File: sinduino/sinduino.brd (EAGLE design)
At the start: 100 x 80 mm, 34 parts, among them IC1 IC_UC_ATMEGA32U4-TQFP44, IC2 TS2940CT5TV, Q1 16000, X1 MINI-USB-32005-301

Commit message: move some things around in the upper right
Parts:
- moved LED4 9.85 mm to (51.8, 18.1)
- moved R3 4.26 mm to (32.4, 27.3), turned to 180 degrees
- moved C4 2.56 mm to (54.0, 21.3)
- moved R6 2.42 mm to (47.9, 21.3), turned to 180 degrees
- moved C3 1.93 mm to (34.3, 25.1)
- moved C9 1.62 mm to (42.2, 25.1)
- moved C8 1.27 mm to (48.3, 24.8)
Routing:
- net VCC: track 109.5 -> 115.7 mm
- net N$18: track 0.00 -> 2.92 mm
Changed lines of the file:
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@@
 <setting verticaltext="up"/>
 </settings>
-<grid distance="12.5" unitdist="mil" unit="mil" style="dots" multiple="1" display="no" altdistance="25" altunitdist="mil" altunit="mil"/>
+<grid distance="12.5" unitdist="mil" unit="mil" style="dots" multiple="1" display="yes" altdistance="25" altunitdist="mil" altunit="mil"/>
 <layers>
 <layer number="1" name="Top" color="4" fill="1" visible="yes" active="yes"/>
@@
 <element name="C1" library="rcl" package="C025-025X050" value="470n" x="12.7" y="27.94" rot="R270"/>
 <element name="C2" library="rcl" package="E2,5-6" value="33u" x="12.7" y="22.225" rot="R90"/>
-<element name="C3" library="rcl" package="C1206" value="100n" x="36.195" y="24.765" rot="MR180"/>
-<element name="C4" library="rcl" package="C1206" value="100n" x="55.245" y="23.495" rot="MR0"/>
+<element name="C3" library="rcl" package="C1206" value="100n" x="34.29" y="25.0825" rot="MR180"/>
+<element name="C4" library="rcl" package="C1206" value="100n" x="53.975" y="21.2725" rot="MR0"/>
 <element name="C5" library="rcl" package="C1206" value="100n" x="42.8625" y="8.89" rot="MR180"/>
 <element name="C6" library="rcl" package="C1206" value="100n" x="24.13" y="10.4775" rot="MR0"/>
 <element name="C7" library="rcl" package="C1206" value="100n" x="23.1775" y="7.62" rot="MR0"/>
-<element name="C8" library="rcl" package="C1206" value="18p" x="48.26" y="23.495" rot="MR0"/>
-<element name="C9" library="rcl" package="C1206" value="18p" x="42.545" y="23.495" rot="MR0"/>
+<element name="C8" library="rcl" package="C1206" value="18p" x="48.26" y="24.765" rot="MR0"/>
+<element name="C9" library="rcl" package="C1206" value="18p" x="42.2275" y="25.0825" rot="MR0"/>
 <element name="C10" library="rcl" package="C1206" value="1u" x="22.86" y="19.05" rot="MR0"/>
 <element name="C11" library="rcl" package="C1206" value="1u" x="15.875" y="6.985" rot="MR180"/>
@@
 <attribute name="REICHELT" value="TASTER 9305" x="28.8925" y="26.035" size="1.778" layer="27" rot="R270" display="off"/>
 </element>
-<element name="R3" library="rcl" package="R1206" value="10k" x="36.195" y="29.21" rot="MR270"/>
+<element name="R3" library="rcl" package="R1206" value="10k" x="32.385" y="27.305" rot="MR180"/>
 <element name="X1" library="con-cypressindustries" package="32005-301" value="MINI-USB-32005-301" x="6" y="18.5" rot="MR180">
 <attribute name="OC_NEWARK" value="unknown" x="6" y="18.5" size="1.778" layer="28" rot="MR180" display="off"/>
@@
 <element name="JP2" library="pinhead" package="1X17" value="" x="30" y="33"/>
 <element name="JP3" library="pinhead" package="1X17" value="" x="30" y="4" rot="R180"/>
-<element name="R6" library="rcl" package="R1206" value="680" x="50.165" y="20.32" rot="MR0"/>
-<element name="LED4" library="led" package="LED3MM" value="yellow" x="55.245" y="27.305" rot="R180"/>
+<element name="R6" library="rcl" package="R1206" value="680" x="47.9425" y="21.2725" rot="MR180"/>
+<element name="LED4" library="led" package="LED3MM" value="yellow" x="51.7525" y="18.0975" rot="R180"/>
 <element name="R5" library="rcl" package="R1206" value="3k9" x="46.6725" y="10.4775" rot="MR90"/>
 <element name="IC2" library="n39" package="TO220V" value="TS2940CT5TV" x="20.32" y="25.0825" rot="R270">
@@
 <wire x1="9.68" y1="33" x2="9.68" y2="31.5875" width="0.4064" layer="16"/>
 <wire x1="9.68" y1="31.5875" x2="8.255" y2="30.1625" width="0.4064" layer="16"/>
-<wire x1="56.645" y1="23.495" x2="56.515" y2="27.305" width="0" layer="19" extent="16-16"/>
-<wire x1="42.53" y1="19.71" x2="56.645" y2="23.495" width="0" layer="19" extent="16-16"/>
+<wire x1="33.807" y1="27.305" x2="33.807" y2="25.9995" width="0.4064" layer="16"/>
+<wire x1="33.807" y1="25.9995" x2="32.89" y2="25.0825" width="0.4064" layer="16"/>
+<wire x1="34.43" y1="22.21" x2="34.43" y2="23.5425" width="0.4064" layer="16"/>
+<wire x1="34.43" y1="23.5425" x2="32.89" y2="25.0825" width="0.4064" layer="16"/>
+<wire x1="53.0225" y1="18.0975" x2="55.375" y2="21.2725" width="0" layer="19" extent="16-16"/>
+<wire x1="42.53" y1="19.71" x2="53.0225" y2="18.0975" width="0" layer="19" extent="16-16"/>
 <wire x1="34.43" y1="19.5075" x2="40.83" y2="19.24" width="0" layer="19" extent="16-16"/>
-<wire x1="34.795" y1="24.765" x2="34.43" y2="22.21" width="0" layer="19" extent="16-16"/>
-<wire x1="36.195" y1="27.788" x2="34.795" y2="24.765" width="0" layer="19" extent="16-16"/>
 <wire x1="32.0925" y1="13.31" x2="32.2325" y2="17.31" width="0" layer="19" extent="16-16"/>
 </signal>
@@
 <contactref element="IC1" pad="P17"/>
 <contactref element="Q1" pad="2"/>
-<wire x1="46.86" y1="23.495" x2="48.768" y2="28.575" width="0" layer="19" extent="16-16"/>
-<wire x1="36.83" y1="22.21" x2="46.86" y2="23.495" width="0" layer="19" extent="16-16"/>
+<wire x1="46.86" y1="24.765" x2="48.768" y2="28.575" width="0" layer="19" extent="16-16"/>
+<wire x1="36.83" y1="22.21" x2="46.86" y2="24.765" width="0" layer="19" extent="16-16"/>
 </signal>
 <signal name="N$4">
@@
 <contactref element="C9" pad="2"/>
 <contactref element="Q1" pad="1"/>
-<wire x1="41.145" y1="23.495" x2="43.942" y2="28.575" width="0" layer="19" extent="16-16"/>
-<wire x1="36.03" y1="22.21" x2="41.145" y2="23.495" width="0" layer="19" extent="16-16"/>
+<wire x1="40.8275" y1="25.0825" x2="43.942" y2="28.575" width="0" layer="19" extent="16-16"/>
+<wire x1="36.03" y1="22.21" x2="40.8275" y2="25.0825" width="0" layer="19" extent="16-16"/>
 </signal>
 <signal name="N$6">
@@
 <wire x1="32.54" y1="31.905" x2="31.1425" y2="30.5075" width="0.4064" layer="16"/>
 <wire x1="31.1425" y1="29.285" x2="31.1425" y2="30.5075" width="0.4064" layer="16"/>
-<wire x1="31.1425" y1="29.285" x2="31.1425" y2="22.785" width="0.4064" layer="16"/>
 <wire x1="33.63" y1="22.21" x2="33.63" y2="23.2025" width="0.4064" layer="16"/>
 <wire x1="33.63" y1="23.2025" x2="33.3375" y2="23.495" width="0.4064" layer="16"/>
 <wire x1="33.3375" y1="23.495" x2="31.8525" y2="23.495" width="0.4064" layer="16"/>
+<wire x1="31.1425" y1="29.285" x2="31.1425" y2="27.4845" width="0.4064" layer="16"/>
+<wire x1="31.1425" y1="27.4845" x2="30.963" y2="27.305" width="0.4064" layer="16"/>
+<wire x1="31.1425" y1="22.785" x2="31.1425" y2="27.1255" width="0.4064" layer="16"/>
+<wire x1="31.1425" y1="27.1255" x2="30.963" y2="27.305" width="0.4064" layer="16"/>
 <wire x1="31.8525" y1="23.495" x2="31.1425" y2="22.785" width="0.4064" layer="16"/>
-<wire x1="32.54" y1="31.905" x2="36.195" y2="30.632" width="0" layer="19" extent="16-16"/>
 </signal>
 <signal name="N$8">
@@
 <contactref element="IC1" pad="P22"/>
 <contactref element="R6" pad="1"/>
-<wire x1="40.83" y1="22.21" x2="51.587" y2="20.32" width="0" layer="19" extent="16-16"/>
+<wire x1="40.83" y1="22.21" x2="46.5205" y2="21.2725" width="0" layer="19" extent="16-16"/>
 </signal>
 <signal name="N$11">
 <contactref element="R6" pad="2"/>
 <contactref element="LED4" pad="K"/>
-<wire x1="48.743" y1="20.32" x2="53.975" y2="27.305" width="0" layer="19" extent="16-16"/>
+<wire x1="50.4825" y1="18.0975" x2="49.3645" y2="21.2725" width="0" layer="19" extent="16-16"/>
 </signal>
 <signal name="D7">
@@
 <contactref element="IC1" pad="P42"/>
 <contactref element="C7" pad="1"/>
-<wire x1="34.43" y1="10.81" x2="34.43" y2="9.3475" width="0.4064" layer="16"/>
-<wire x1="34.43" y1="9.3475" x2="33.9725" y2="8.89" width="0.4064" layer="16"/>
-<wire x1="33.9725" y1="8.89" x2="27.6225" y2="8.89" width="0.4064" layer="16"/>
-<wire x1="27.6225" y1="8.89" x2="26.3525" y2="7.62" width="0.4064" layer="16"/>
-<wire x1="26.3525" y1="7.62" x2="24.5775" y2="7.62" width="0.4064" layer="16"/>
-<wire x1="22.38" y1="4" x2="22.38" y2="5.235" width="0.4064" layer="16"/>
-<wire x1="22.38" y1="5.235" x2="24.5775" y2="7.4325" width="0.4064" layer="16"/>
-<wire x1="24.5775" y1="7.4325" x2="24.5775" y2="7.62" width="0.4064" layer="16"/>
+<wire x1="34.43" y1="10.81" x2="34.43" y2="9.3475" width="0.3048" layer="16"/>
+<wire x1="34.43" y1="9.3475" x2="33.9725" y2="8.89" width="0.3048" layer="16"/>
+<wire x1="33.9725" y1="8.89" x2="27.6225" y2="8.89" width="0.3048" layer="16"/>
+<wire x1="27.6225" y1="8.89" x2="26.3525" y2="7.62" width="0.3048" layer="16"/>
+<wire x1="26.3525" y1="7.62" x2="24.5775" y2="7.62" width="0.3048" layer="16"/>
+<wire x1="22.38" y1="4" x2="22.38" y2="5.235" width="0.3048" layer="16"/>
+<wire x1="22.38" y1="5.235" x2="24.5775" y2="7.4325" width="0.3048" layer="16"/>
+<wire x1="24.5775" y1="7.4325" x2="24.5775" y2="7.62" width="0.3048" layer="16"/>
 </signal>
 <signal name="A5">
@@
 <contactref element="LED3" pad="K"/>
 <contactref element="R4" pad="1"/>
-<wire x1="51.9045" y1="10.4775" x2="51.7525" y2="13.335" width="0" layer="19" extent="16-16"/>
+<wire x1="51.7525" y1="13.335" x2="51.7525" y2="10.6295" width="0.4064" layer="16"/>
+<wire x1="51.7525" y1="10.6295" x2="51.9045" y2="10.4775" width="0.4064" layer="16"/>
 </signal>
 </signals>

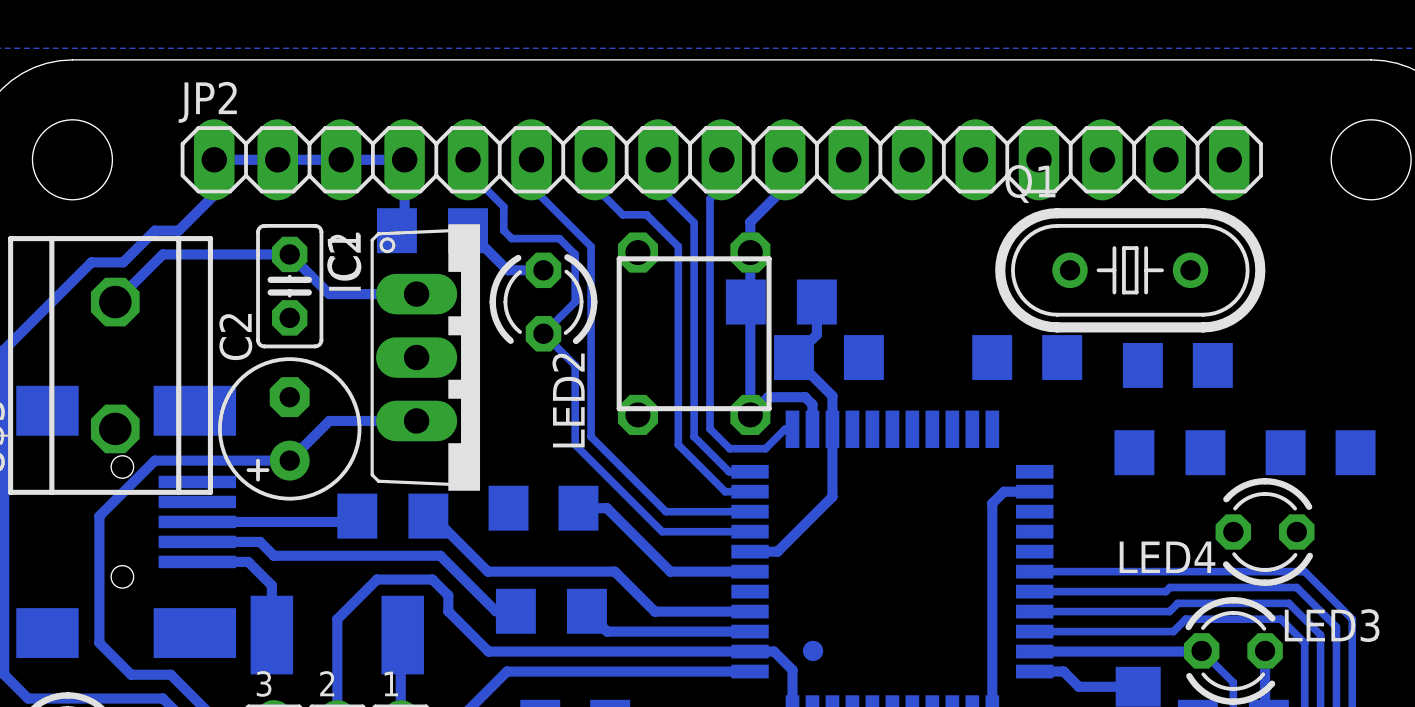
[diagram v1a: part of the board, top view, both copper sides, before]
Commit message: routed all the stuff around the xtal
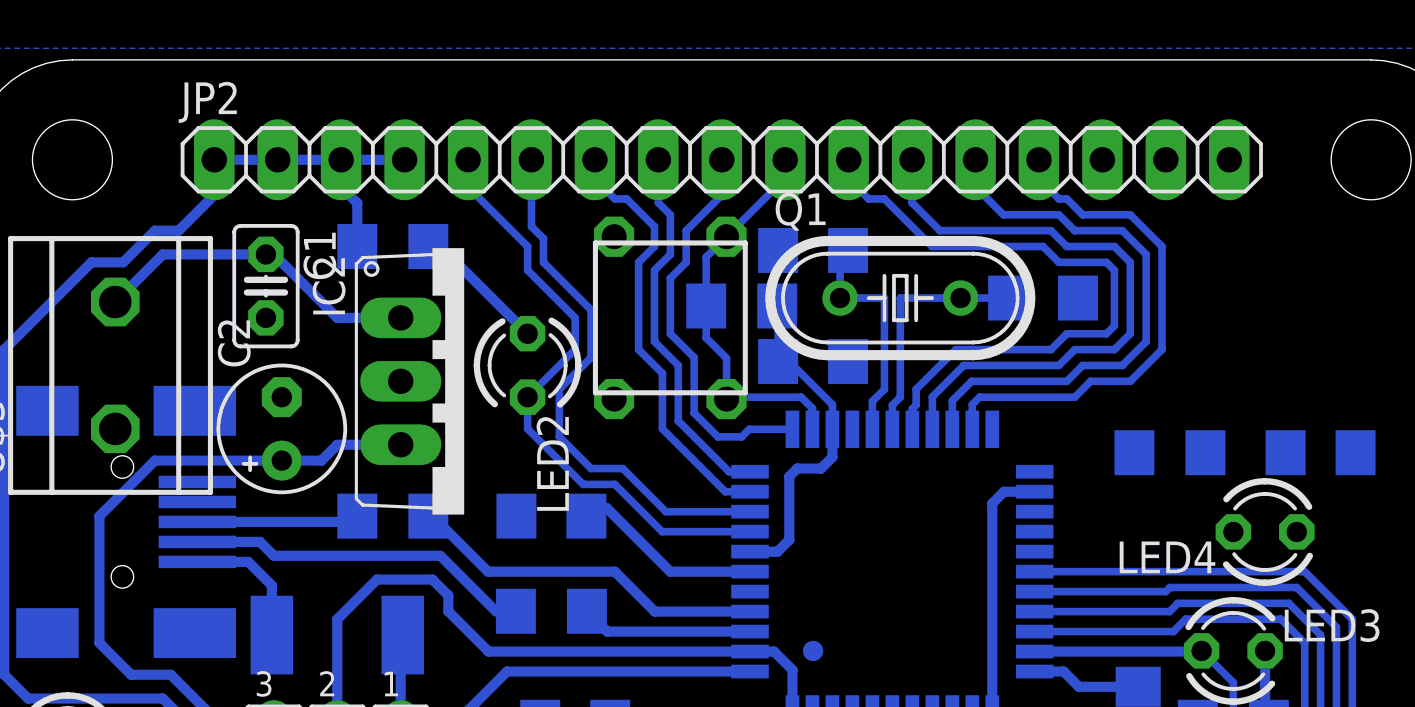
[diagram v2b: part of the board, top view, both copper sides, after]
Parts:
- C2: device rcl:E2,5-6 -> rcl:E2,5-5
- moved C9 9.58 mm to (33.7, 29.4), turned to 180 degrees
- moved Q1 9.27 mm to (37.1, 27.5)
- moved C8 6.03 mm to (42.9, 27.5)
- moved LED2 2.62 mm to (22.2, 24.8)
- moved R2 1.71 mm to (16.8, 29.5)
- moved R3 1.60 mm to (30.8, 27.1)
- moved IC2 1.14 mm to (19.7, 24.1)
- moved U$1 1.14 mm to (27.9, 26.7)
- moved C1 0.95 mm to (11.7, 27.9)
- moved C3 0.65 mm to (33.7, 24.9)
- moved C10 0.45 mm to (23.2, 18.7)
- moved C2 0.32 mm to (12.4, 22.2)
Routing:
- net D3: track 0.00 -> 25.8 mm
- net D2: track 0.00 -> 24.6 mm
- net D0: track 0.00 -> 22.4 mm
- net D1: track 0.00 -> 20.4 mm
- net N$3: track 0.00 -> 9.70 mm
- net N$4: track 0.00 -> 9.27 mm
- net D15: track 19.7 -> 21.5 mm
- net N$17: track 3.68 -> 5.42 mm
- net VCC: track 115.7 -> 117.0 mm
- net !RESET: track 14.8 -> 16.2 mm
- net N$16: track 27.9 -> 26.9 mm
- net D11: track 14.9 -> 15.8 mm
- net D17: track 14.5 -> 15.0 mm

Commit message: routing complete
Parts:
- moved C4 7.30 mm to (46.7, 21.3)
- moved R6 4.27 mm to (51.1, 24.1)
- moved LED4 3.19 mm to (52.1, 21.3), turned to 0 degrees
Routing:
- net VCC: track 117.0 -> 148.9 mm, vias 0 -> 4
- net D4: track 0.00 -> 31.8 mm
- net D12: track 0.00 -> 31.2 mm
- net D6: track 0.00 -> 30.7 mm
- net N$2: track 0.00 -> 9.66 mm
- net N$11: track 0.00 -> 3.19 mm

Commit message: dimension
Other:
- board size 100 x 80 mm -> 60 x 37 mm
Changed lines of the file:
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@@
 <setting verticaltext="up"/>
 </settings>
-<grid distance="0.3175" unitdist="mm" unit="mm" style="dots" multiple="1" display="yes" altdistance="25" altunitdist="mil" altunit="mil"/>
+<grid distance="50" unitdist="mil" unit="mil" style="dots" multiple="1" display="no" altdistance="25" altunitdist="mil" altunit="mil"/>
 <layers>
 <layer number="1" name="Top" color="4" fill="1" visible="yes" active="yes"/>
@@
 <layer number="21" name="tPlace" color="7" fill="1" visible="yes" active="yes"/>
 <layer number="22" name="bPlace" color="7" fill="1" visible="yes" active="yes"/>
-<layer number="23" name="tOrigins" color="15" fill="1" visible="yes" active="yes"/>
-<layer number="24" name="bOrigins" color="15" fill="1" visible="yes" active="yes"/>
-<layer number="25" name="tNames" color="7" fill="1" visible="yes" active="yes"/>
-<layer number="26" name="bNames" color="7" fill="1" visible="yes" active="yes"/>
-<layer number="27" name="tValues" color="7" fill="1" visible="yes" active="yes"/>
-<layer number="28" name="bValues" color="7" fill="1" visible="yes" active="yes"/>
+<layer number="23" name="tOrigins" color="15" fill="1" visible="no" active="yes"/>
+<layer number="24" name="bOrigins" color="15" fill="1" visible="no" active="yes"/>
+<layer number="25" name="tNames" color="7" fill="1" visible="no" active="yes"/>
+<layer number="26" name="bNames" color="7" fill="1" visible="no" active="yes"/>
+<layer number="27" name="tValues" color="7" fill="1" visible="no" active="yes"/>
+<layer number="28" name="bValues" color="7" fill="1" visible="no" active="yes"/>
 <layer number="29" name="tStop" color="7" fill="3" visible="no" active="yes"/>
 <layer number="30" name="bStop" color="7" fill="6" visible="no" active="yes"/>
@@
 <board>
 <plain>
-<wire x1="0" y1="0" x2="100" y2="0" width="0" layer="20"/>
-<wire x1="100" y1="0" x2="100" y2="80" width="0" layer="20"/>
-<wire x1="100" y1="80" x2="0" y2="80" width="0" layer="20"/>
-<wire x1="0" y1="80" x2="0" y2="0" width="0" layer="20"/>
 <circle x="33.655" y="13.335" radius="0.4064" width="0" layer="16"/>
 </plain>
@@
 <contactref element="U$3" pad="1"/>
 <contactref element="LED1" pad="K"/>
+<contactref element="R4" pad="2"/>
 <polygon width="0.4064" layer="16">
-<vertex x="-0.635" y="37.465"/>
-<vertex x="60.325" y="37.465"/>
-<vertex x="60.325" y="-0.635"/>
-<vertex x="-0.635" y="-0.635"/>
-<vertex x="-0.635" y="0"/>
+<vertex x="4" y="0"/>
+<vertex x="56" y="0" curve="90"/>
+<vertex x="60" y="4"/>
+<vertex x="60" y="33" curve="90"/>
+<vertex x="56" y="37"/>
+<vertex x="4" y="37" curve="90"/>
+<vertex x="0" y="33"/>
+<vertex x="0" y="4" curve="90"/>
 </polygon>
-<contactref element="R4" pad="2"/>
 </signal>
 <signal name="N$3">

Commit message: drc
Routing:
- net UV: track 5.24 -> 4.16 mm
- net VCC: track 148.9 -> 147.9 mm
- net N$16: track 26.9 -> 27.5 mm
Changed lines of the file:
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@@
 <layer number="21" name="tPlace" color="7" fill="1" visible="yes" active="yes"/>
 <layer number="22" name="bPlace" color="7" fill="1" visible="yes" active="yes"/>
-<layer number="23" name="tOrigins" color="15" fill="1" visible="no" active="yes"/>
-<layer number="24" name="bOrigins" color="15" fill="1" visible="no" active="yes"/>
+<layer number="23" name="tOrigins" color="15" fill="1" visible="yes" active="yes"/>
+<layer number="24" name="bOrigins" color="15" fill="1" visible="yes" active="yes"/>
 <layer number="25" name="tNames" color="7" fill="1" visible="no" active="yes"/>
 <layer number="26" name="bNames" color="7" fill="1" visible="no" active="yes"/>
@@
 <param name="dpMaxLengthDifference" value="10mm"/>
 <param name="dpGapFactor" value="2.5"/>
-<param name="checkGrid" value="1"/>
+<param name="checkGrid" value="0"/>
 <param name="checkAngle" value="1"/>
 <param name="checkFont" value="1"/>
@@
 <wire x1="12.22" y1="33" x2="9.68" y2="33" width="0.4064" layer="16"/>
 <contactref element="R2" pad="2"/>
-<wire x1="14.605" y1="9.8425" x2="14.605" y2="6.48" width="0.4064" layer="16"/>
-<wire x1="14.605" y1="6.48" x2="14.475" y2="6.985" width="0.4064" layer="16"/>
 <wire x1="12.217" y1="6.985" x2="12.217" y2="6.833" width="0.4064" layer="16"/>
-<wire x1="12.217" y1="6.985" x2="14.475" y2="6.985" width="0.4064" layer="16"/>
 <wire x1="14.605" y1="9.8425" x2="14.605" y2="14.605" width="0.4064" layer="16"/>
 <wire x1="32.83" y1="10.81" x2="32.83" y2="12.5725" width="0.4064" layer="16"/>
@@
 <wire x1="19.05" y1="14.9225" x2="20.6625" y2="13.31" width="0.4064" layer="16"/>
 <wire x1="1.27" y1="25.4" x2="1.27" y2="12.3825" width="0.4064" layer="16"/>
-<wire x1="12.217" y1="6.985" x2="12.065" y2="6.985" width="0.4064" layer="16"/>
-<wire x1="12.065" y1="6.985" x2="7.62" y2="11.43" width="0.4064" layer="16"/>
 <wire x1="7.62" y1="11.43" x2="2.2225" y2="11.43" width="0.4064" layer="16"/>
 <wire x1="2.2225" y1="11.43" x2="1.27" y2="12.3825" width="0.4064" layer="16"/>
@@
 <wire x1="29.68" y1="17.31" x2="29.5275" y2="17.4625" width="0.4064" layer="16"/>
 <wire x1="29.5275" y1="17.4625" x2="28.575" y2="17.4625" width="0.4064" layer="16"/>
+<wire x1="14.605" y1="9.8425" x2="14.605" y2="7.115" width="0.4064" layer="16"/>
+<wire x1="14.605" y1="7.115" x2="14.475" y2="6.985" width="0.4064" layer="16"/>
+<wire x1="7.62" y1="11.43" x2="12.065" y2="6.985" width="0.4064" layer="16"/>
+<wire x1="12.065" y1="6.985" x2="12.217" y2="6.985" width="0.4064" layer="16"/>
+<wire x1="14.475" y1="6.985" x2="12.217" y2="6.985" width="0.4064" layer="16"/>
 </signal>
 <signal name="GND" class="1">
@@
 <contactref element="F1" pad="2"/>
 <contactref element="JP1" pad="1"/>
-<wire x1="17.145" y1="9.8425" x2="17.145" y2="14.525" width="0.4064" layer="16"/>
-<wire x1="17.145" y1="14.525" x2="17.225" y2="13.97" width="0.4064" layer="16"/>
+<wire x1="17.145" y1="9.8425" x2="17.145" y2="13.89" width="0.4064" layer="16"/>
+<wire x1="17.145" y1="13.89" x2="17.225" y2="13.97" width="0.4064" layer="16"/>
 </signal>
 <signal name="N$10" class="1">
@@
 <contactref element="C2" pad="+"/>
 <contactref element="JP1" pad="3"/>
-<wire x1="12.3825" y1="20.955" x2="7.3025" y2="20.955" width="0.4064" layer="16"/>
-<wire x1="7.3025" y1="20.955" x2="5.08" y2="18.7325" width="0.4064" layer="16"/>
-<wire x1="5.08" y1="18.7325" x2="5.08" y2="13.6525" width="0.4064" layer="16"/>
+<wire x1="12.3825" y1="20.955" x2="7.14375" y2="20.955" width="0.4064" layer="16"/>
 <wire x1="12.065" y1="9.8425" x2="10.4775" y2="9.8425" width="0.4064" layer="16"/>
 <wire x1="10.4775" y1="9.8425" x2="7.9375" y2="12.3825" width="0.4064" layer="16"/>
@@
 <wire x1="12.3825" y1="20.955" x2="13.97" y2="20.955" width="0.4064" layer="16"/>
 <wire x1="13.97" y1="20.955" x2="14.605" y2="21.59" width="0.4064" layer="16"/>
+<wire x1="7.14375" y1="20.955" x2="6.82625" y2="20.6375" width="0.4064" layer="16"/>
+<wire x1="6.82625" y1="20.6375" x2="6.82625" y2="19.84375" width="0.4064" layer="16"/>
+<wire x1="6.82625" y1="19.84375" x2="4.445" y2="17.4625" width="0.4064" layer="16"/>
+<wire x1="4.445" y1="17.4625" x2="4.445" y2="15.875" width="0.4064" layer="16"/>
+<wire x1="4.445" y1="15.875" x2="5.08" y2="15.24" width="0.4064" layer="16"/>
+<wire x1="5.08" y1="15.24" x2="5.08" y2="13.6525" width="0.4064" layer="16"/>
 </signal>
 <signal name="N$14">
@@
 </signal>
 </signals>
+<errors>
+</errors>
 </board>
 </drawing>
